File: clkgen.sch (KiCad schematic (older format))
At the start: 15 parts

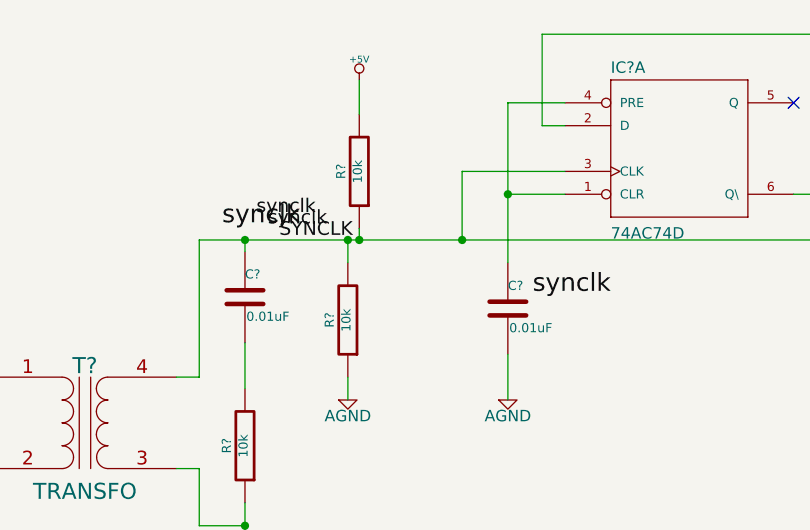
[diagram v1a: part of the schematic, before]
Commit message: Finished filters page, started demod
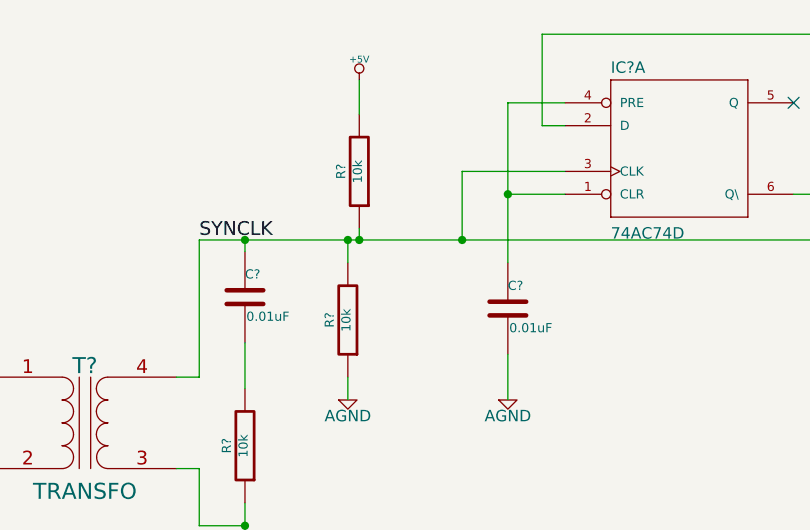
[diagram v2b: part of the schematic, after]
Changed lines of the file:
@@
 LIBS:cmos4000
 LIBS:adc-dac
-LIBS:memory
 LIBS:special
 LIBS:analog_switches
@@
 LIBS:tsop
 LIBS:varistor
-LIBS:vishay
-LIBS:vishay_tsal4400_bpw85c
-LIBS:vishay-1
 LIBS:v-reg
-LIBS:v-reg-2
-LIBS:v-reg-fairchild
-LIBS:v-reg-lowdrop
 LIBS:si570
 LIBS:blackrock_components
@@
 Sheet 3 5
 Title ""
-Date "16 oct 2014"
+Date "19 oct 2014"
 Rev ""
 Comp ""
@@
 	6100 1800 6100 1900
 Connection ~ 6100 1800
-Text Label 5700 1700 0    60   ~ 0
-synclk
-Text Label 5750 1750 0    60   ~ 0
-synclk
-Text Label 5800 1800 0    60   ~ 0
+Text Label 5450 1800 0    60   ~ 0
 SYNCLK
-Text Label 5550 1750 0    79   ~ 0
-synclk
 Connection ~ 6150 1800
 Wire Wire Line
@@
 	8250 2750 10350 2750
 Connection ~ 8250 1600
-Text Label 7250 2050 2    79   ~ 0
-synclk
 $EndSCHEMATC
